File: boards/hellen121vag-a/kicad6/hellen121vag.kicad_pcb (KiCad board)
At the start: 2 copper layers, 164 x 118 mm, 68 parts, among them J1 USB_B_Mini, M1 Module-can-0.1, M10 Module-can-0.1, M11 Module-vr-0.1, M2 Module-power5-0.1, M3 Module-mcu-0.1, M4 Module-input-0.1, M5 Module-knock-0.1, M6 Module-output-0.1, M7 Module-ign8-0.1, M8 Module-power12-0.1, M9 Module-wbo-0.1, P1 368255-2

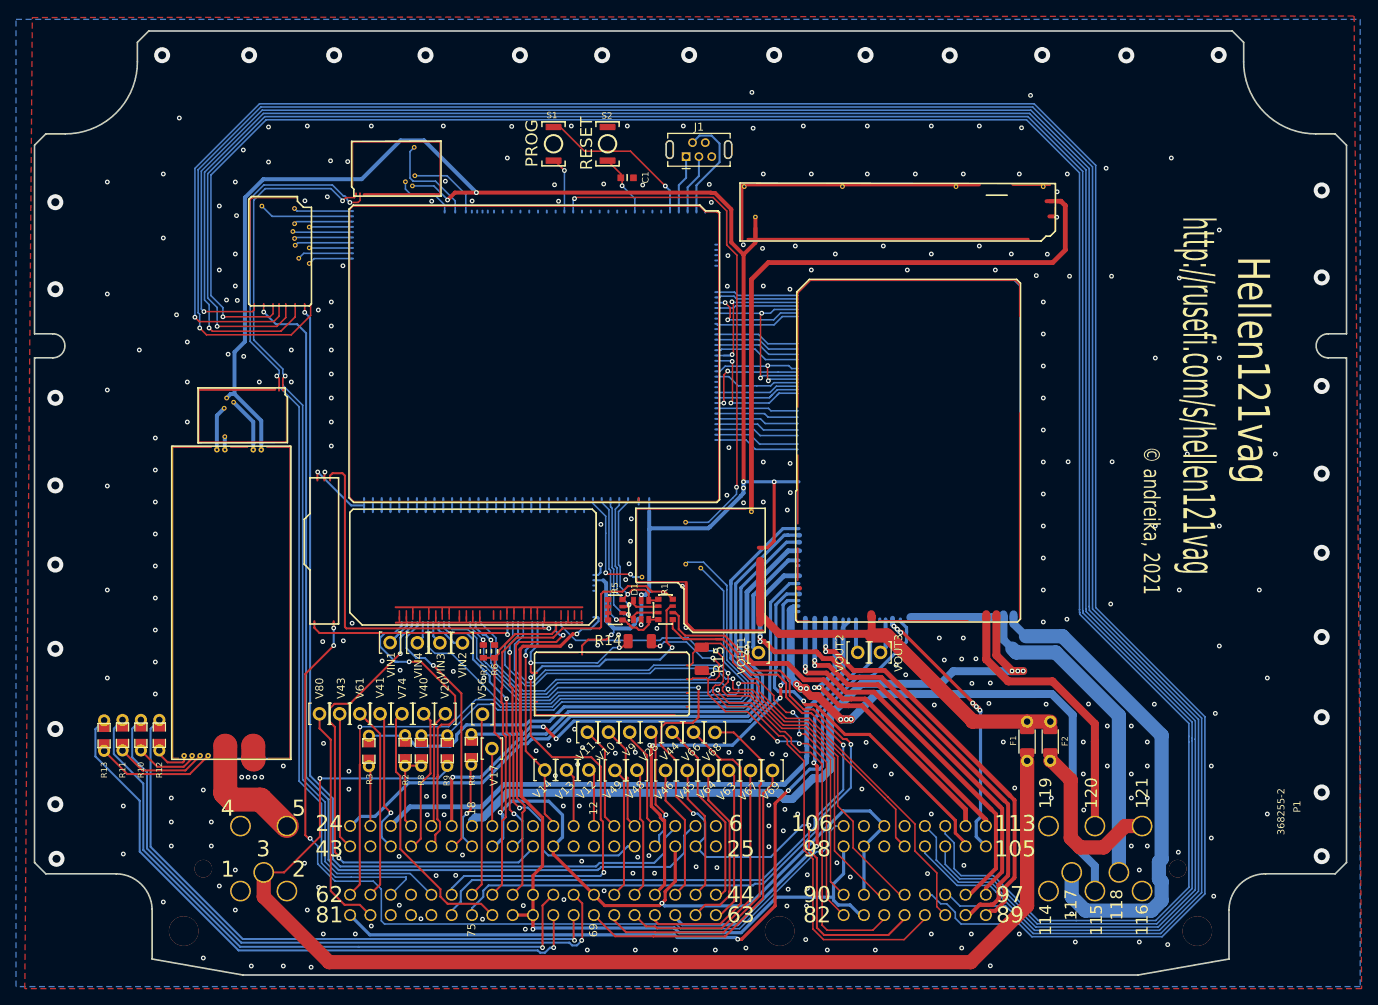
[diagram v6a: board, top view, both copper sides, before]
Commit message: Dinput4 + proto areas
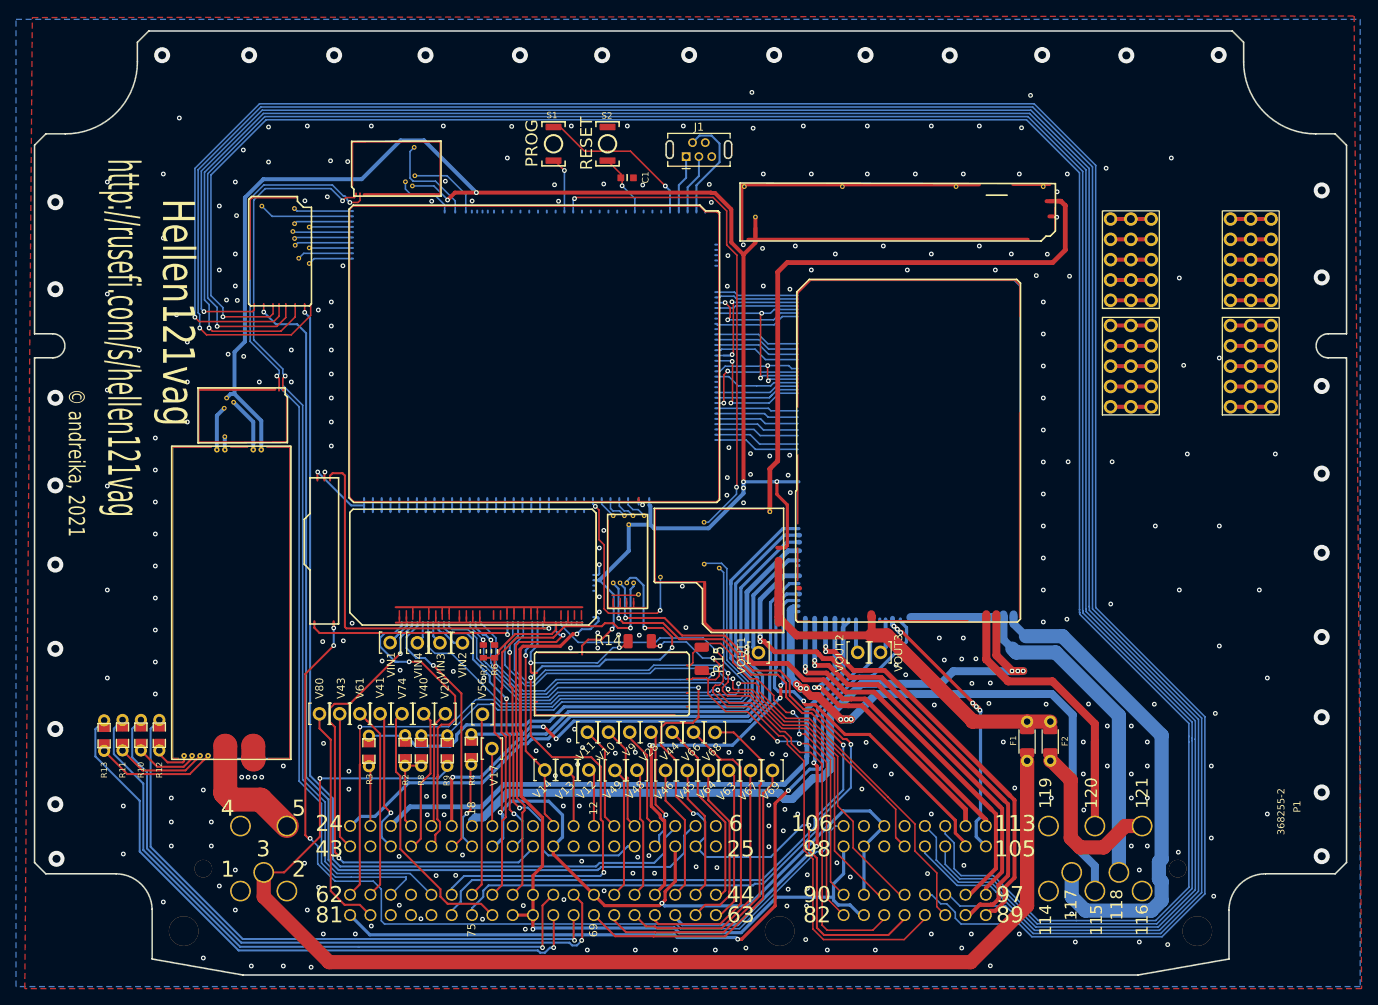
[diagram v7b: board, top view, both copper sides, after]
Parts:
- removed D1: D_TVS_Array_4, hellen-one-common:SOT23-6
- removed R1, R5: Res_Array_4, hellen-one-common:R0603-4
- added G1: PROTO_AREA, hellen-one-common:PROTO_AREA, F.Cu at (180.2, 39.3)
- added G2: PROTO_AREA, hellen-one-common:PROTO_AREA, F.Cu at (195.2, 26.0)
- added G3: PROTO_AREA, hellen-one-common:PROTO_AREA, F.Cu at (195.2, 39.3)
- added G4: PROTO_AREA, hellen-one-common:PROTO_AREA, F.Cu at (180.2, 26.0)
- added M12: Module-dinput4-0.1, hellen-one-dinput4-0.1:dinput4, F.Cu at (117.2, 52.7)
- moved M8 2.31 mm to (123.1, 67.7)
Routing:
- net /D4: track 22.5 -> 2.67 mm, vias 1 -> 0
- net /D3: track 21.2 -> 3.29 mm, vias 1 -> 0
- net /D2: track 19.6 -> 3.09 mm, vias 1 -> 0
- net /D1: track 19.0 -> 3.29 mm, vias 1 -> 0
- net /VIGN: track 14.8 -> 25.9 mm
- net /IN_D4: track 93.7 -> 103.6 mm, vias 1 -> 2
- net /IN_D3: track 92.7 -> 102.0 mm, vias 1 -> 2
- net /IN_D2: track 76.9 -> 84.3 mm, vias 3 -> 4
- net +5V: track 231.5 -> 225.0 mm, vias 7 -> 6
- net Net-(G3-Pad14): track 0.00 -> 5.08 mm
- net Net-(G3-Pad13): track 0.00 -> 5.08 mm
- net Net-(G3-Pad12): track 0.00 -> 5.08 mm
- net Net-(G3-Pad10): track 0.00 -> 5.08 mm
- net Net-(G3-Pad1): track 0.00 -> 5.08 mm
- net Net-(G2-Pad14): track 0.00 -> 5.08 mm
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
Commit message: Conector silk
https://github.com/rusefi/hellen121vag/issues/13
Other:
- board text added: "10"
- board text added: "100"
- board text added: "101"
- board text added: "102"
- board text added: "103"
- board text added: "104"
- board text added: "107"
- board text added: "108"
- board text added: "109"
- board text added: "11"
- board text added: "110"
- board text added: "111"
- board text added: "112"
- board text added: "13"
- board text added: "14"
- board text added: "15"
- board text added: "16"
- board text added: "17"
- board text added: "19"
- board text added: "20"
- board text added: "21"
- board text added: "22"
- board text added: "23"
- board text added: "26"
- board text added: "27"
- board text added: "28"
- board text added: "29"
- board text added: "30"
- board text added: "31"
- board text added: "32"
- board text added: "33"
- board text added: "34"
- board text added: "35"
- board text added: "36"
- board text added: "37"
- board text added: "38"
- board text added: "39"
- board text added: "40"
- board text added: "41"
- board text added: "42"
- board text added: "45"
- board text added: "46"
- board text added: "47"
- board text added: "48"
- board text added: "49"
- board text added: "50"
- board text added: "51"
- board text added: "52"
- board text added: "53"
- board text added: "54"
- board text added: "55"
- board text added: "56"
- board text added: "57"
- board text added: "58"
- board text added: "59"
- board text added: "60"
- board text added: "61"
- board text added: "64"
- board text added: "65"
- board text added: "66"
- board text added: "67"
- board text added: "68"
- board text added: "7"
- board text added: "70"
- board text added: "71"
- board text added: "72"
- board text added: "73"
- board text added: "74"
- board text added: "76"
- board text added: "77"
- board text added: "78"
- board text added: "79"
- board text added: "8"
- board text added: "80"
- board text added: "83"
- board text added: "84"
- board text added: "85"
- board text added: "86"
- board text added: "87"
- board text added: "88"
- board text added: "9"
- board text added: "91"
- board text added: "92"
- board text added: "93"
- board text added: "94"
- board text added: "95"
- board text added: "96"
- board text added: "99"
